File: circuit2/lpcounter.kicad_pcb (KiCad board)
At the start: 2 copper layers, 81 x 51 mm, 26 parts, among them IC1 ATTINY85V-P, M1 SYN115, P1 CONN_01X08, P2 CONN_02X01, P3 Hole_3.5mm, P4 Hole_3.5mm, P5 Hole_3.5mm, P6 Hole_3.5mm, P7 BAT+, P8 BAT-

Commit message: optimizing PCB
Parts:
- moved P5 50.6 mm to (44.5, 137.5)
- moved P6 39.0 mm to (76.0, 168.5)
- moved P4 24.0 mm to (118.5, 137.5)
- moved BT1 20.5 mm to (97.0, 135.9)
- moved P8 12.1 mm to (44.0, 130.5)
- moved P7 3.12 mm to (118.5, 131.0)
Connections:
- D1 pad 2: Net-(D1-Pad2) -> /VBAT
- P4 pad 1: GND -> /VBAT
- P7 pad 1: Net-(D1-Pad2) -> /VBAT
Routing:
- net /VBAT: track 0.00 -> 24.2 mm
- net GND: track 68.1 -> 50.6 mm
- net +3V3: track 147.5 -> 158.3 mm
- net Net-(D1-Pad2): track 10.8 -> 0.00 mm
- net /IN3: track 68.6 -> 66.7 mm
- net /IN2: track 48.4 -> 46.9 mm
- net /IN1: track 40.4 -> 39.3 mm
- net /IN0: track 53.0 -> 52.1 mm

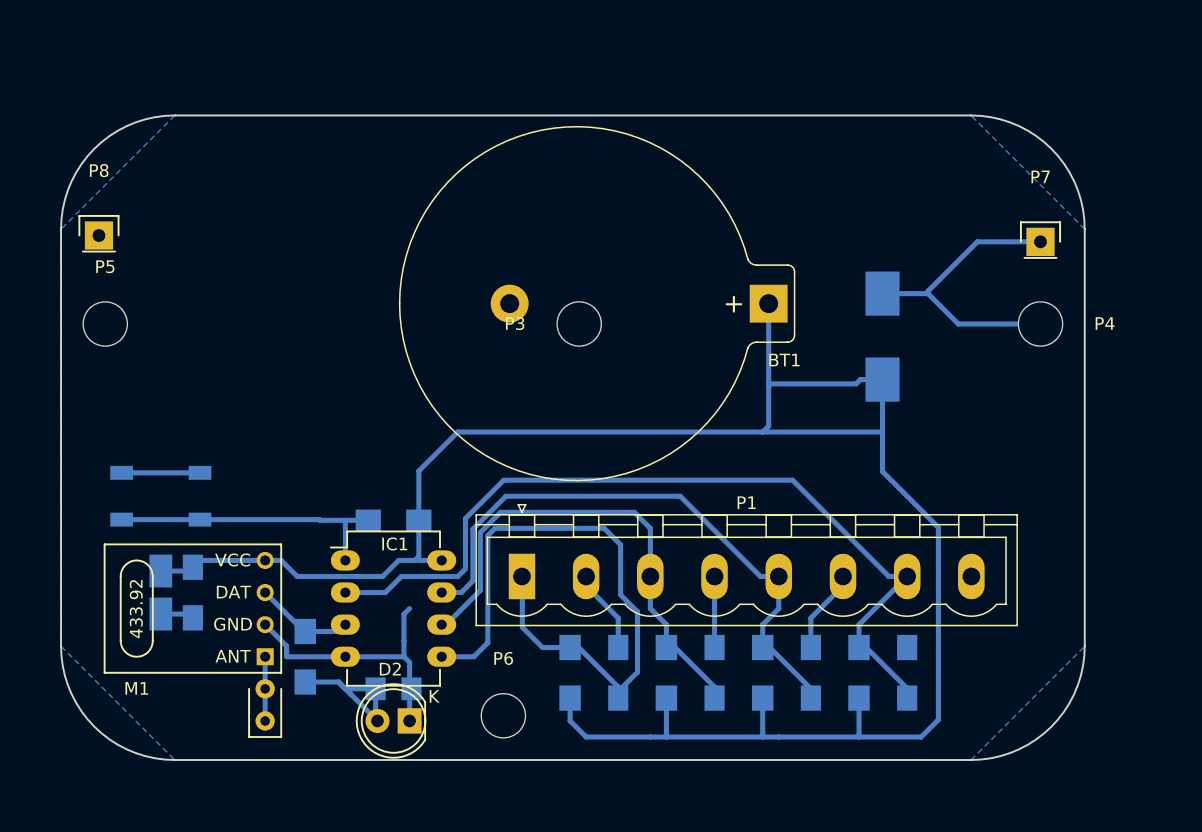
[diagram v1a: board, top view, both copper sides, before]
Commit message: changing pushbutton to jumper
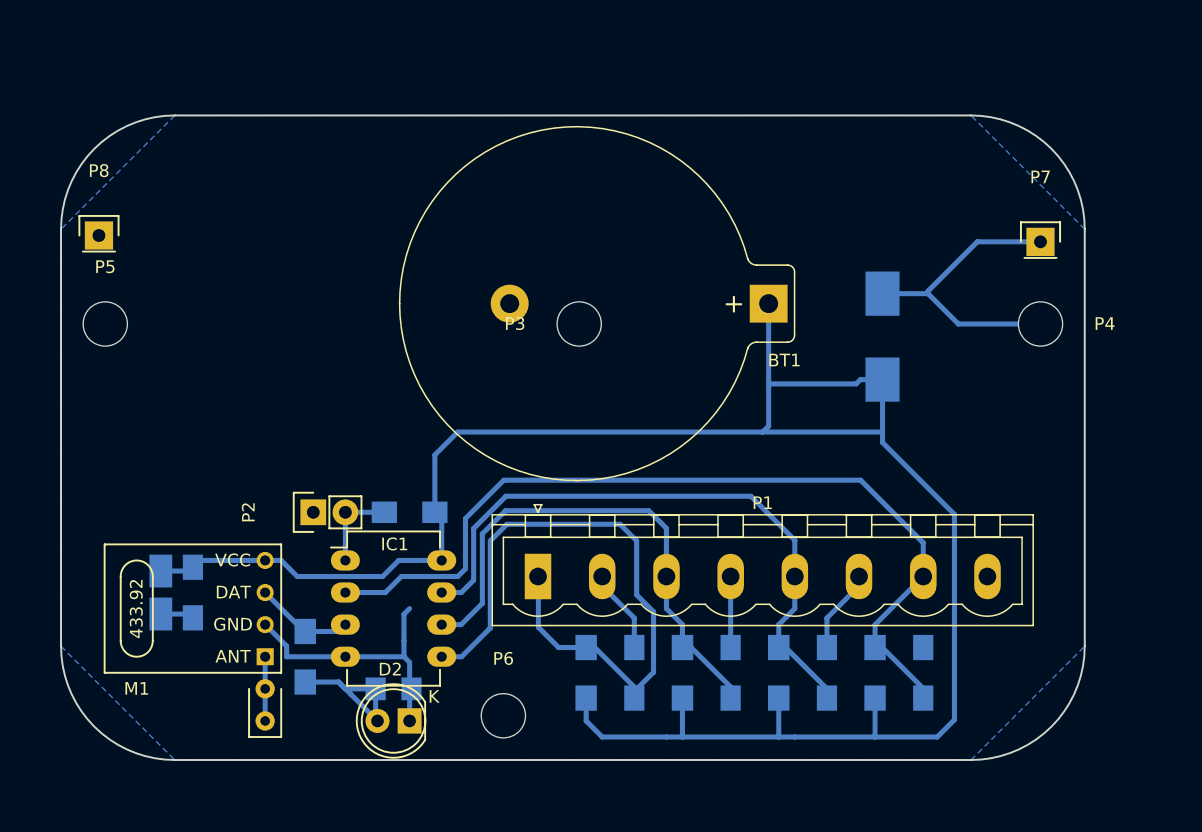
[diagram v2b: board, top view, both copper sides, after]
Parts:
- P2: footprint Buttons_Switches_SMD:SW_SPST_SKQG -> Pin_Headers:Pin_Header_Straight_1x02; moved to F.Cu
- moved P2 12.1 mm to (61.0, 152.4), turned to 90 degrees
- moved R6 1.42 mm to (68.6, 152.4)
- moved C2 1.27 mm to (94.0, 165.1)
- moved R3 1.27 mm to (97.8, 165.1)
- moved C1 1.27 mm to (86.4, 165.1)
- moved C3 1.27 mm to (101.6, 165.1)
- moved C4 1.27 mm to (109.2, 165.1)
- moved P1 1.27 mm to (78.7, 157.5)
- moved R1 1.27 mm to (82.5, 165.1)
- moved R2 1.27 mm to (90.2, 165.1)
- moved R4 1.27 mm to (105.4, 165.1)
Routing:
- net /RESETn: track 22.9 -> 6.97 mm
- net GND: track 50.6 -> 44.4 mm
- net /IN2: track 46.9 -> 49.8 mm
- net /IN3: track 66.7 -> 69.6 mm
- net /IN1: track 39.3 -> 41.3 mm
- net /IN0: track 52.1 -> 52.9 mm

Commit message: increase PCB to fully fit into ABC box, multiple battery contacts
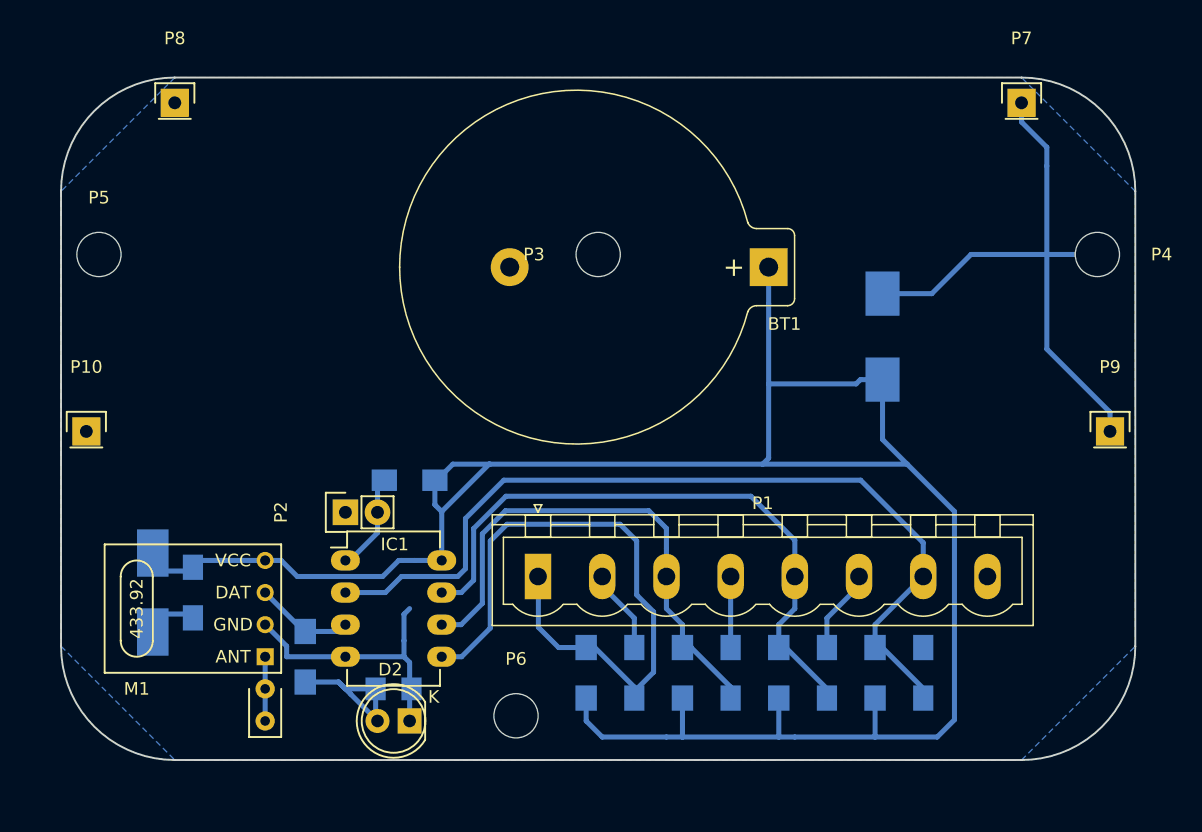
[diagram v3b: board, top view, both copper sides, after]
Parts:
- added P10: BAT-, Pin_Headers:Pin_Header_Straight_1x01, F.Cu at (43.0, 146.0)
- added P9: BAT+, Pin_Headers:Pin_Header_Straight_1x01, F.Cu at (124.0, 146.0)
- C5: footprint Capacitors_Tantalum_SMD:Tantalum_Case-R_EIA-2012-12_Hand -> Capacitors_Tantalum_SMD:Tantalum_Case-U_EIA-6032-15_Hand
- moved P8 12.1 mm to (50.0, 120.0)
- moved P7 11.1 mm to (117.0, 120.0)
- moved P4 7.11 mm to (123.0, 132.0)
- moved P3 5.70 mm to (83.5, 132.0)
- moved P5 5.52 mm to (44.0, 132.0)
- moved BT1 2.89 mm to (97.0, 133.0)
- moved P2 2.54 mm to (63.5, 152.4)
- moved R6 2.54 mm to (68.6, 149.9)
- moved P6 1.00 mm to (77.0, 168.5)
- moved C5 0.64 mm to (48.3, 158.8)
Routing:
- net /VBAT: track 24.2 -> 47.6 mm
- net +3V3: track 158.4 -> 168.9 mm
- net /RESETn: track 6.97 -> 7.91 mm
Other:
- board size 81 x 51 mm -> 85 x 54 mm

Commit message: optimizing PCB
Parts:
- moved D1 0.68 mm to (106.7, 138.5)
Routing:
- net /IN0: track 52.9 -> 23.7 mm
- net /VBAT: track 47.6 -> 46.5 mm
- net +3V3: track 168.9 -> 168.2 mm

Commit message: optimizing PCB
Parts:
- moved C6 1.91 mm to (53.3, 158.8)
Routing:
- net +3V3: track 168.2 -> 169.9 mm
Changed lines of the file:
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@@
   )
   (module Capacitors_SMD:C_1206_HandSoldering (layer B.Cu)
-    (at 51.435 158.75 270)
+    (at 53.34 158.75 270)
     (descr "Capacitor SMD 1206, hand soldering")
     (tags "capacitor 1206")
@@
   (segment (start 109.22 157.48) (end 105.41 161.29) (width 0.4) (layer B.Cu) (net 5))
   (segment (start 105.41 161.29) (end 105.41 163.1) (width 0.4) (layer B.Cu) (net 5))
+  (segment (start 48.26 155.625) (end 53.34 155.625) (width 0.4) (layer B.Cu) (net 6))
+  (segment (start 53.34 155.625) (end 56.565 155.625) (width 0.4) (layer B.Cu) (net 6))
+  (segment (start 53.34 156.75) (end 53.34 155.625) (width 0.4) (layer B.Cu) (net 6))
+  (segment (start 56.565 155.625) (end 57.15 156.21) (width 0.4) (layer B.Cu) (net 6))
   (segment (start 106.68 148.59) (end 106.905219 148.59) (width 0.4) (layer B.Cu) (net 6))
   (segment (start 106.905219 148.59) (end 111.690932 153.375713) (width 0.4) (layer B.Cu) (net 6))
@@
   (segment (start 59.69 157.48) (end 66.449 157.48) (width 0.4) (layer B.Cu) (net 6))
   (segment (start 57.15 156.21) (end 58.42 156.21) (width 0.4) (layer B.Cu) (net 6))
-  (segment (start 57.15 156.21) (end 51.975 156.21) (width 0.4) (layer B.Cu) (net 6))
-  (segment (start 51.975 156.21) (end 51.435 156.75) (width 0.4) (layer B.Cu) (net 6))
   (segment (start 66.449 157.48) (end 67.719 156.21) (width 0.4) (layer B.Cu) (net 6))
-  (segment (start 51.135 157.05) (end 51.435 156.75) (width 0.4) (layer B.Cu) (net 6))
-  (segment (start 48.895 157.05) (end 51.135 157.05) (width 0.4) (layer B.Cu) (net 6))
   (segment (start 65.89014 166.37) (end 65.89014 168.76014) (width 0.4) (layer B.Cu) (net 7))
   (segment (start 65.89014 168.76014) (end 66.04 168.91) (width 0.4) (layer B.Cu) (net 7))

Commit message: increase clearance in design rules
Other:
- net class Default: clearance 0.19 -> 0.26
- rule trace_clearance: 0.19 -> 0.26
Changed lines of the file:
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@@
   (setup
     (last_trace_width 0.4)
-    (trace_clearance 0.19)
+    (trace_clearance 0.26)
     (zone_clearance 0.508)
     (zone_45_only no)
@@
   (net 11 /VBAT)
   (net_class Default "This is the default net class."
-    (clearance 0.19)
+    (clearance 0.26)
     (trace_width 0.4)
     (via_dia 0.6)

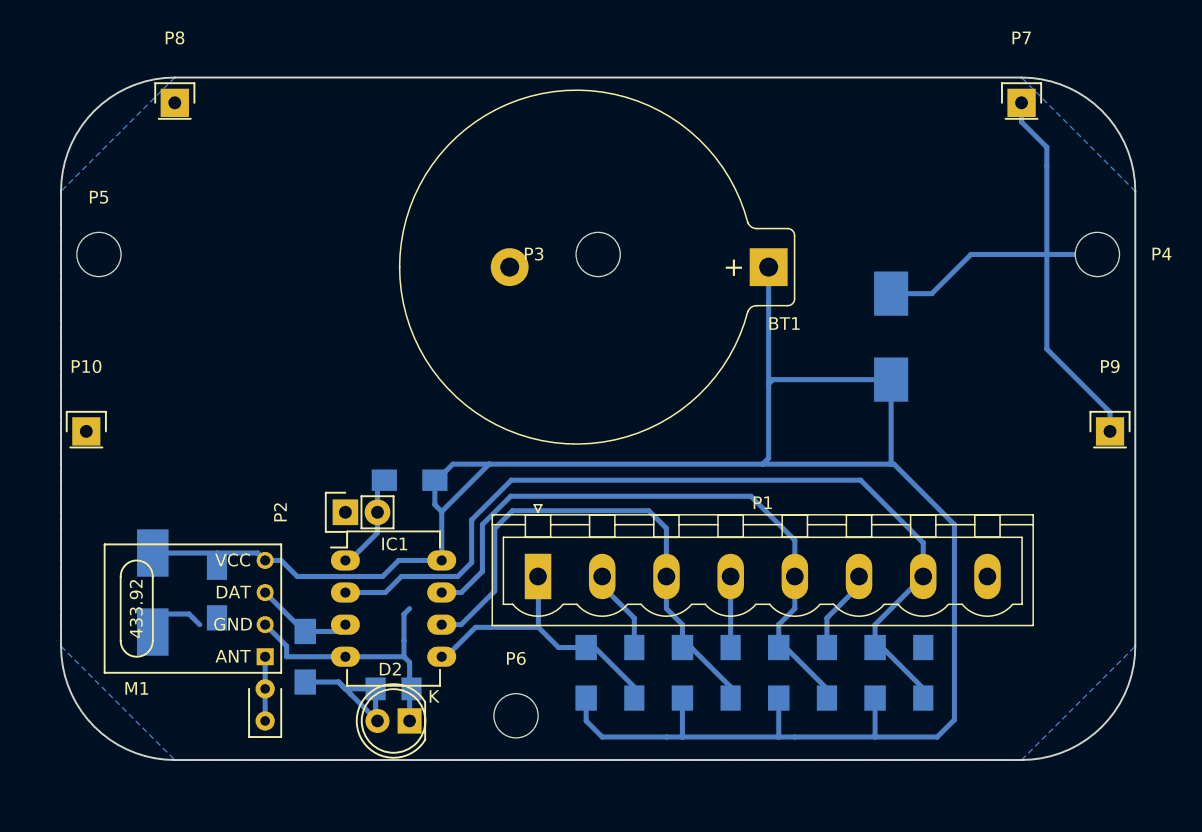
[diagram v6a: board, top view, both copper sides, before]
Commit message: preparation for fabrication moving electronic parts away from the edge
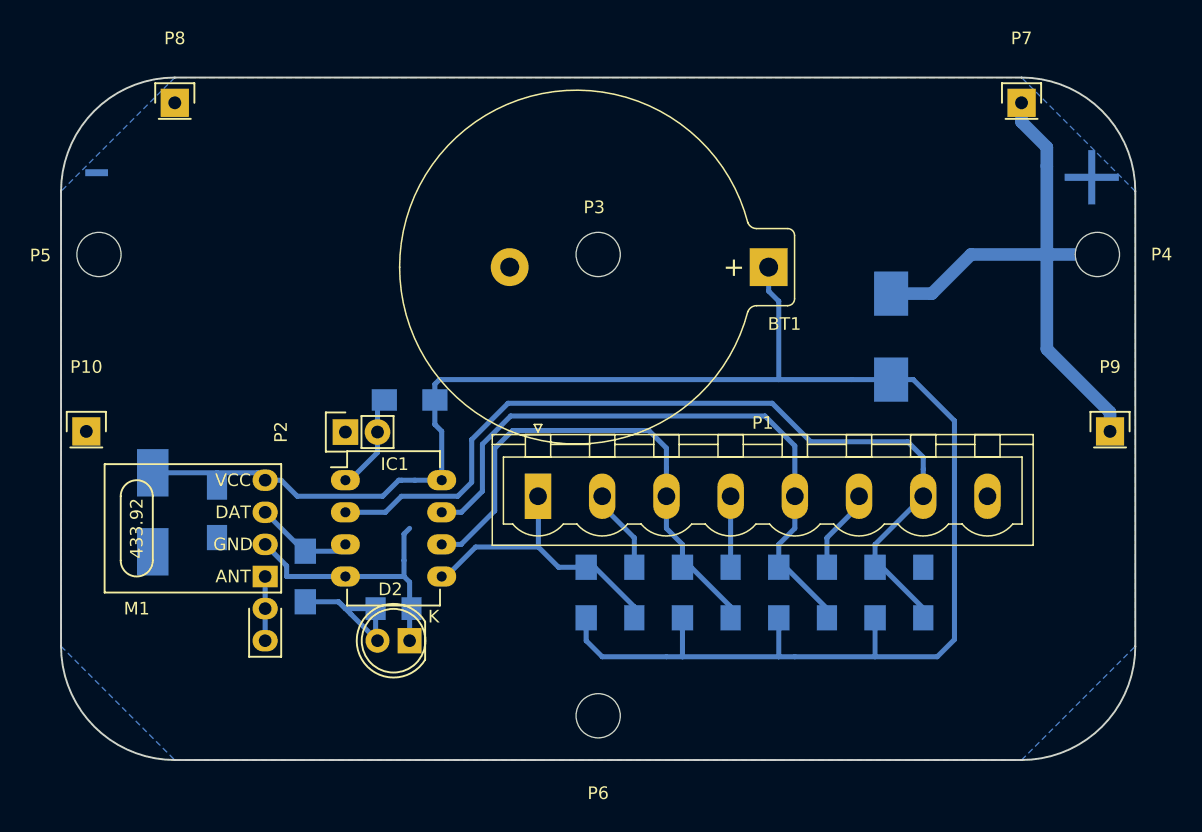
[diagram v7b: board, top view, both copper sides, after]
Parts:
- moved P6 6.50 mm to (83.5, 168.5)
- moved R5 6.35 mm to (60.3, 157.5)
- moved R6 6.35 mm to (68.6, 143.5)
- moved C1 6.35 mm to (86.4, 158.8)
- moved C2 6.35 mm to (94.0, 158.8)
- moved C3 6.35 mm to (101.6, 158.8)
- moved C4 6.35 mm to (109.2, 158.8)
- moved C5 6.35 mm to (48.3, 152.4)
- moved C6 6.35 mm to (53.3, 152.4)
- moved D2 6.35 mm to (68.6, 162.6)
- moved D3 6.35 mm to (67.3, 160.0)
- moved IC1 6.35 mm to (63.5, 149.9)
- moved M1 6.35 mm to (57.1, 154.9)
- moved P1 6.35 mm to (78.7, 151.1)
- moved P2 6.35 mm to (63.5, 146.1)
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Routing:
- net +3V3: track 169.9 -> 143.8 mm
- net GND: track 44.4 -> 41.0 mm
- net /IN2: track 49.6 -> 50.3 mm
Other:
- net class Power added: clearance 0.5, trace_width 1, via_dia 0.6, via_drill 0.4
- board text added: "+"
- board text added: "-"

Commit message: holes update
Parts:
- P3, P4, P5, P6: footprint Mounting_Holes:MountingHole_3.5mm -> Mounting_Holes:MountingHole_3.5mm_Pad
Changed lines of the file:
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@@
     (links 53)
     (no_connects 0)
-    (area 27.150001 107.3 129.316191 175.76)
+    (area 40.924999 117.924999 126.075001 172.075001)
     (thickness 1.6)
     (drawings 33)
@@
     (mod_text_size 1 1)
     (mod_text_width 0.15)
-    (pad_size 1.524 1.524)
-    (pad_drill 0.762)
+    (pad_size 6 6)
+    (pad_drill 3.5)
     (pad_to_mask_clearance 0.2)
     (aux_axis_origin 0 0)
@@
     )
   )
-  (module Mounting_Holes:MountingHole_3.5mm (layer F.Cu)
-    (at 83.5 132)
-    (descr "Mounting Hole 3.5mm, no annular")
-    (tags "mounting hole 3.5mm no annular")
-    (fp_text reference P3 (at -0.315 -3.73) (layer F.SilkS)
-      (effects (font (size 1 1) (thickness 0.15)))
-    )
-    (fp_text value Hole_3.5mm (at 0 4.5) (layer F.Fab)
-      (effects (font (size 1 1) (thickness 0.15)))
-    )
-    (fp_circle (center 0 0) (end 3.5 0) (layer Cmts.User) (width 0.15))
-    (fp_circle (center 0 0) (end 3.75 0) (layer F.CrtYd) (width 0.05))
-    (pad 1 np_thru_hole circle (at 0 0) (size 3.5 3.5) (drill 3.5) (layers *.Cu *.Mask)
-      (net 1 GND))
-  )
-  (module Mounting_Holes:MountingHole_3.5mm (layer F.Cu)
-    (at 123 132)
-    (descr "Mounting Hole 3.5mm, no annular")
-    (tags "mounting hole 3.5mm no annular")
-    (fp_text reference P4 (at 5.08 0) (layer F.SilkS)
-      (effects (font (size 1 1) (thickness 0.15)))
-    )
-    (fp_text value Hole_3.5mm (at 0 4.5) (layer F.Fab)
-      (effects (font (size 1 1) (thickness 0.15)))
-    )
-    (fp_circle (center 0 0) (end 3.5 0) (layer Cmts.User) (width 0.15))
-    (fp_circle (center 0 0) (end 3.75 0) (layer F.CrtYd) (width 0.05))
-    (pad 1 np_thru_hole circle (at 0 0) (size 3.5 3.5) (drill 3.5) (layers *.Cu *.Mask)
-      (net 11 /VBAT))
-  )
-  (module Mounting_Holes:MountingHole_3.5mm (layer F.Cu)
-    (at 44 132)
-    (descr "Mounting Hole 3.5mm, no annular")
-    (tags "mounting hole 3.5mm no annular")
-    (fp_text reference P5 (at -4.63 0.08) (layer F.SilkS)
-      (effects (font (size 1 1) (thickness 0.15)))
-    )
-    (fp_text value Hole_3.5mm (at 0 4.5) (layer F.Fab)
-      (effects (font (size 1 1) (thickness 0.15)))
-    )
-    (fp_circle (center 0 0) (end 3.5 0) (layer Cmts.User) (width 0.15))
-    (fp_circle (center 0 0) (end 3.75 0) (layer F.CrtYd) (width 0.05))
-    (pad 1 np_thru_hole circle (at 0 0) (size 3.5 3.5) (drill 3.5) (layers *.Cu *.Mask)
-      (net 1 GND))
-  )
-  (module Mounting_Holes:MountingHole_3.5mm (layer F.Cu)
-    (at 83.5 168.5)
-    (descr "Mounting Hole 3.5mm, no annular")
-    (tags "mounting hole 3.5mm no annular")
-    (fp_text reference P6 (at 0 6.125) (layer F.SilkS)
-      (effects (font (size 1 1) (thickness 0.15)))
-    )
-    (fp_text value Hole_3.5mm (at 0 4.5) (layer F.Fab)
-      (effects (font (size 1 1) (thickness 0.15)))
-    )
-    (fp_circle (center 0 0) (end 3.5 0) (layer Cmts.User) (width 0.15))
-    (fp_circle (center 0 0) (end 3.75 0) (layer F.CrtYd) (width 0.05))
-    (pad 1 np_thru_hole circle (at 0 0) (size 3.5 3.5) (drill 3.5) (layers *.Cu *.Mask)
-      (net 1 GND))
-  )
   (module Pin_Headers:Pin_Header_Straight_1x01 (layer F.Cu)
     (at 117 120)
@@
     )
   )
-  (gr_text + (at 122.555 125.73) (layer B.Cu)
+  (module Mounting_Holes:MountingHole_3.5mm_Pad (layer F.Cu)
+    (at 83.5 132)
+    (descr "Mounting Hole 3.5mm")
+    (tags "mounting hole 3.5mm")
+    (fp_text reference P3 (at 0 -4.5) (layer F.SilkS)
+      (effects (font (size 1 1) (thickness 0.15)))
+    )
+    (fp_text value Hole_3.5mm (at 0 4.5) (layer F.Fab)
+      (effects (font (size 1 1) (thickness 0.15)))
+    )
+    (fp_circle (center 0 0) (end 3.5 0) (layer Cmts.User) (width 0.15))
+    (fp_circle (center 0 0) (end 3.75 0) (layer F.CrtYd) (width 0.05))
+    (pad 1 thru_hole circle (at 0 0) (size 7 7) (drill 3.5) (layers *.Cu *.Mask)
+      (net 1 GND))
+  )
+  (module Mounting_Holes:MountingHole_3.5mm_Pad (layer F.Cu)
+    (at 123 132)
+    (descr "Mounting Hole 3.5mm")
+    (tags "mounting hole 3.5mm")
+    (fp_text reference P4 (at 0 -4.5) (layer F.SilkS)
+      (effects (font (size 1 1) (thickness 0.15)))
+    )
+    (fp_text value Hole_3.5mm (at 0 4.5) (layer F.Fab)
+      (effects (font (size 1 1) (thickness 0.15)))
+    )
+    (fp_circle (center 0 0) (end 3.5 0) (layer Cmts.User) (width 0.15))
+    (fp_circle (center 0 0) (end 3.75 0) (layer F.CrtYd) (width 0.05))
+    (pad 1 thru_hole circle (at 0 0) (size 6 6) (drill 3.5) (layers *.Cu *.Mask)
+      (net 11 /VBAT))
+  )
+  (module Mounting_Holes:MountingHole_3.5mm_Pad (layer F.Cu)
+    (at 44 132)
+    (descr "Mounting Hole 3.5mm")
+    (tags "mounting hole 3.5mm")
+    (fp_text reference P5 (at 0 -4.5) (layer F.SilkS)
+      (effects (font (size 1 1) (thickness 0.15)))
+    )
+    (fp_text value Hole_3.5mm (at 0 4.5) (layer F.Fab)
+      (effects (font (size 1 1) (thickness 0.15)))
+    )
+    (fp_circle (center 0 0) (end 3.5 0) (layer Cmts.User) (width 0.15))
+    (fp_circle (center 0 0) (end 3.75 0) (layer F.CrtYd) (width 0.05))
+    (pad 1 thru_hole circle (at 0 0) (size 6 6) (drill 3.5) (layers *.Cu *.Mask)
+      (net 1 GND))
+  )
+  (module Mounting_Holes:MountingHole_3.5mm_Pad (layer F.Cu)
+    (at 83.5 168.5)
+    (descr "Mounting Hole 3.5mm")
+    (tags "mounting hole 3.5mm")
+    (fp_text reference P6 (at 0 -4.5) (layer F.SilkS)
+      (effects (font (size 1 1) (thickness 0.15)))
+    )
+    (fp_text value Hole_3.5mm (at 0 4.5) (layer F.Fab)
+      (effects (font (size 1 1) (thickness 0.15)))
+    )
+    (fp_circle (center 0 0) (end 3.5 0) (layer Cmts.User) (width 0.15))
+    (fp_circle (center 0 0) (end 3.75 0) (layer F.CrtYd) (width 0.05))
+    (pad 1 thru_hole circle (at 0 0) (size 7 7) (drill 3.5) (layers *.Cu *.Mask)
+      (net 1 GND))
+  )
+  (gr_text + (at 122.555 124.5) (layer B.Cu)
     (effects (font (size 5 5) (thickness 1)) (justify mirror))
   )
-  (gr_text - (at 43.815 125.095) (layer B.Cu)
+  (gr_text - (at 43.815 124.5) (layer B.Cu)
     (effects (font (size 5 5) (thickness 1)) (justify mirror))
   )
